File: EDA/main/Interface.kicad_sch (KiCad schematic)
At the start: 16 parts, among them J1 12402012E212A, U1 TF03-TD9P

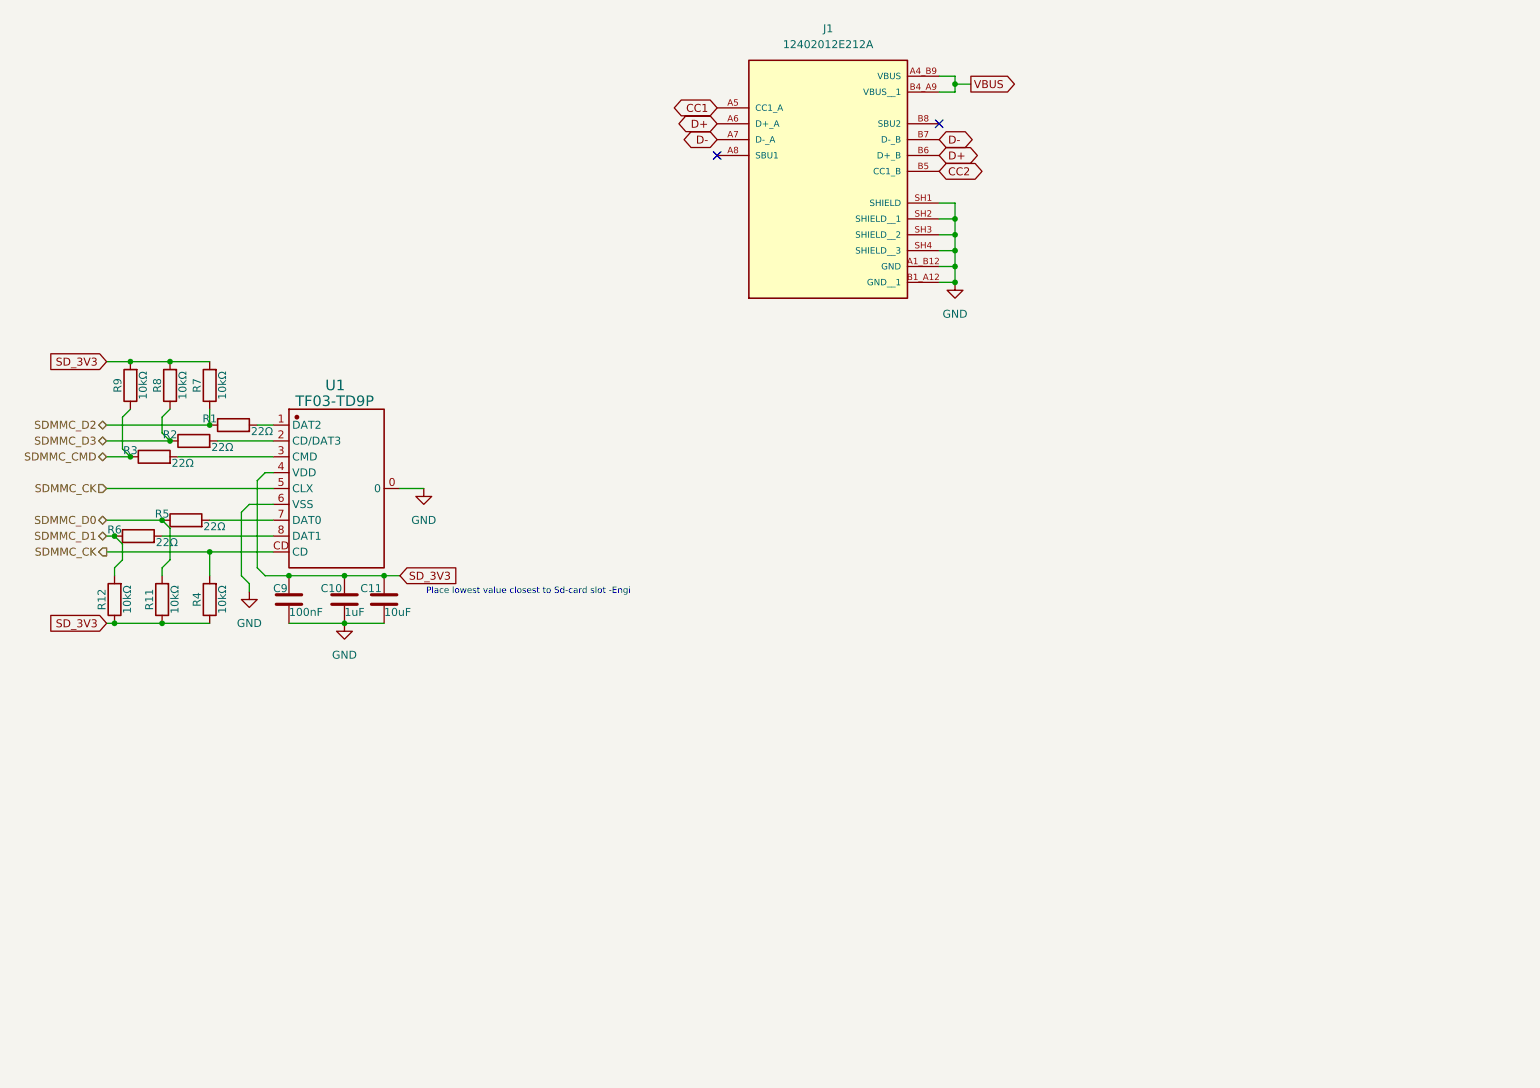
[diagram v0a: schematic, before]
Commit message: Project restructure, and added a bottom assembly PCB.
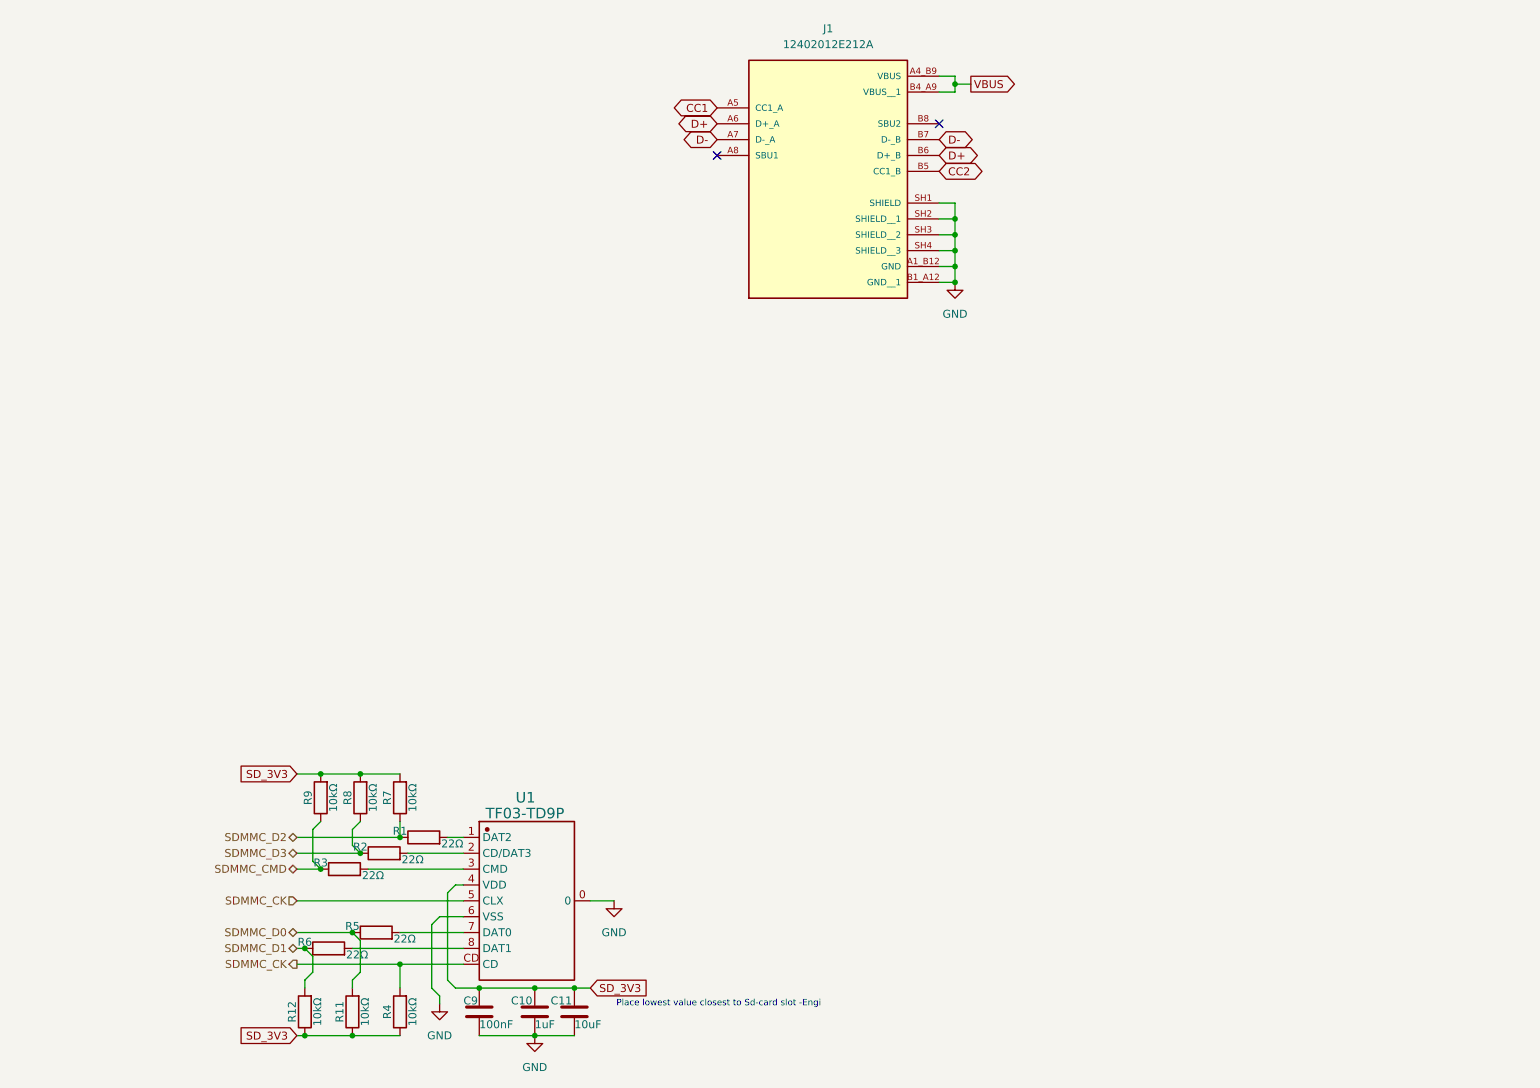
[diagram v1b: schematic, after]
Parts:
- C10, C11: footprint (none) -> Capacitor_SMD:C_0603_1608Metric
- C9: footprint (none) -> Capacitor_SMD:C_0402_1005Metric
- R1, R11, R12, R2, R3, R4, R5, R6, R7, R8, R9: footprint (none) -> Resistor_SMD:R_0402_1005Metric
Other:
- moved on the sheet: C10, C11, C9, R1, R11, R12, R2, R3, R4, R5, R6, R7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

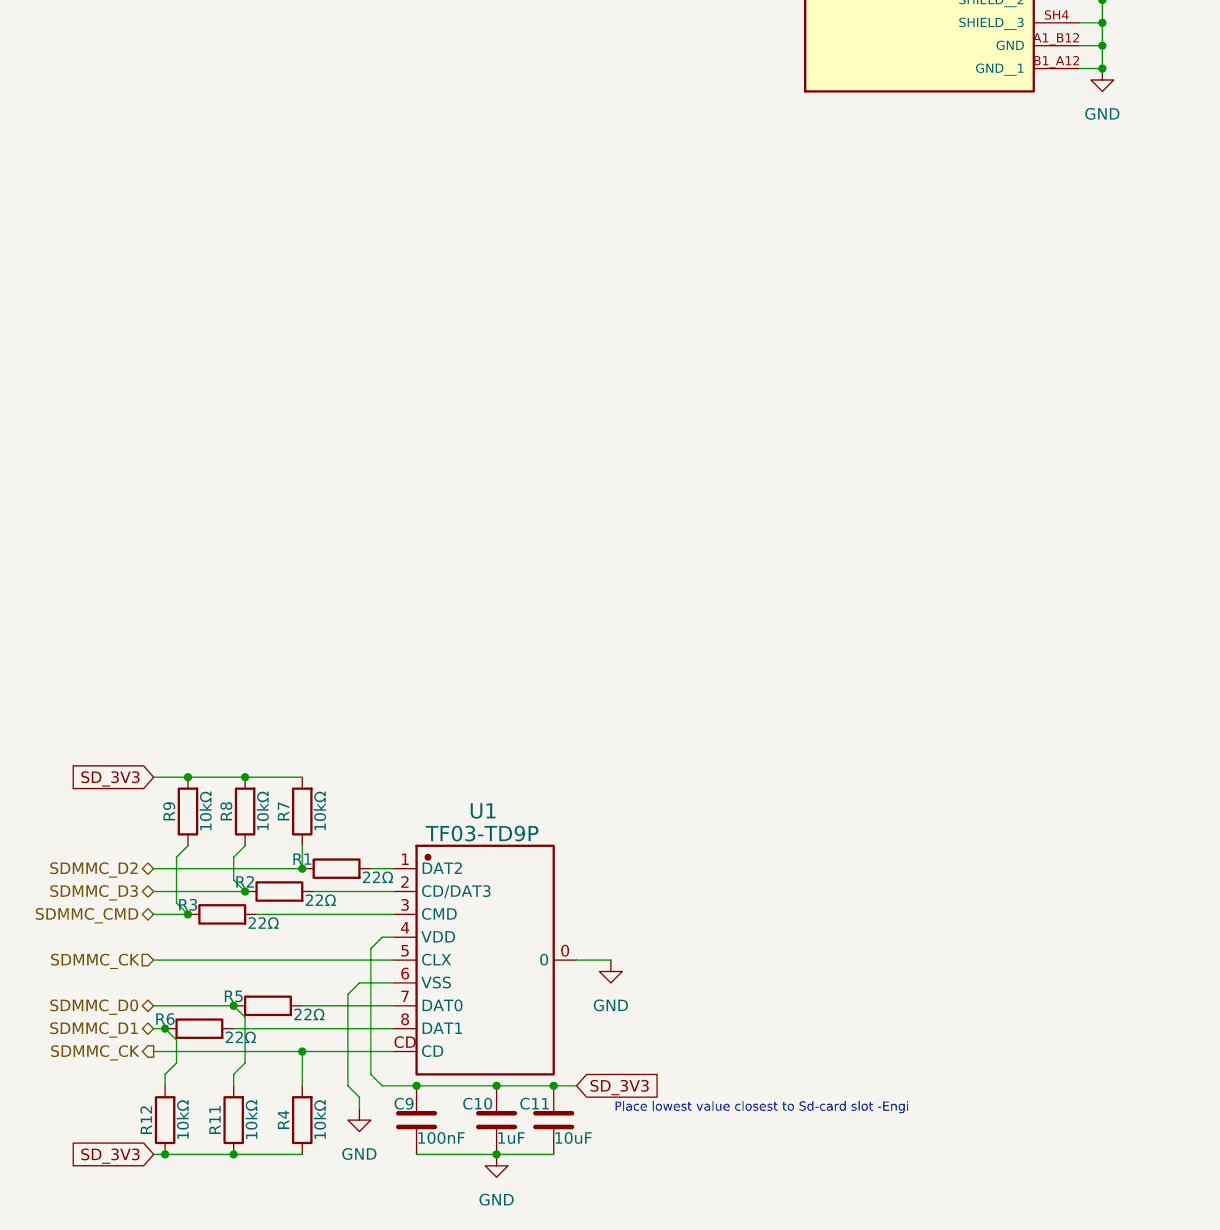
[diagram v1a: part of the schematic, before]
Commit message: Assigned CS and INT from sensors, and added SWD to PWR-MCU and CORE-MCU
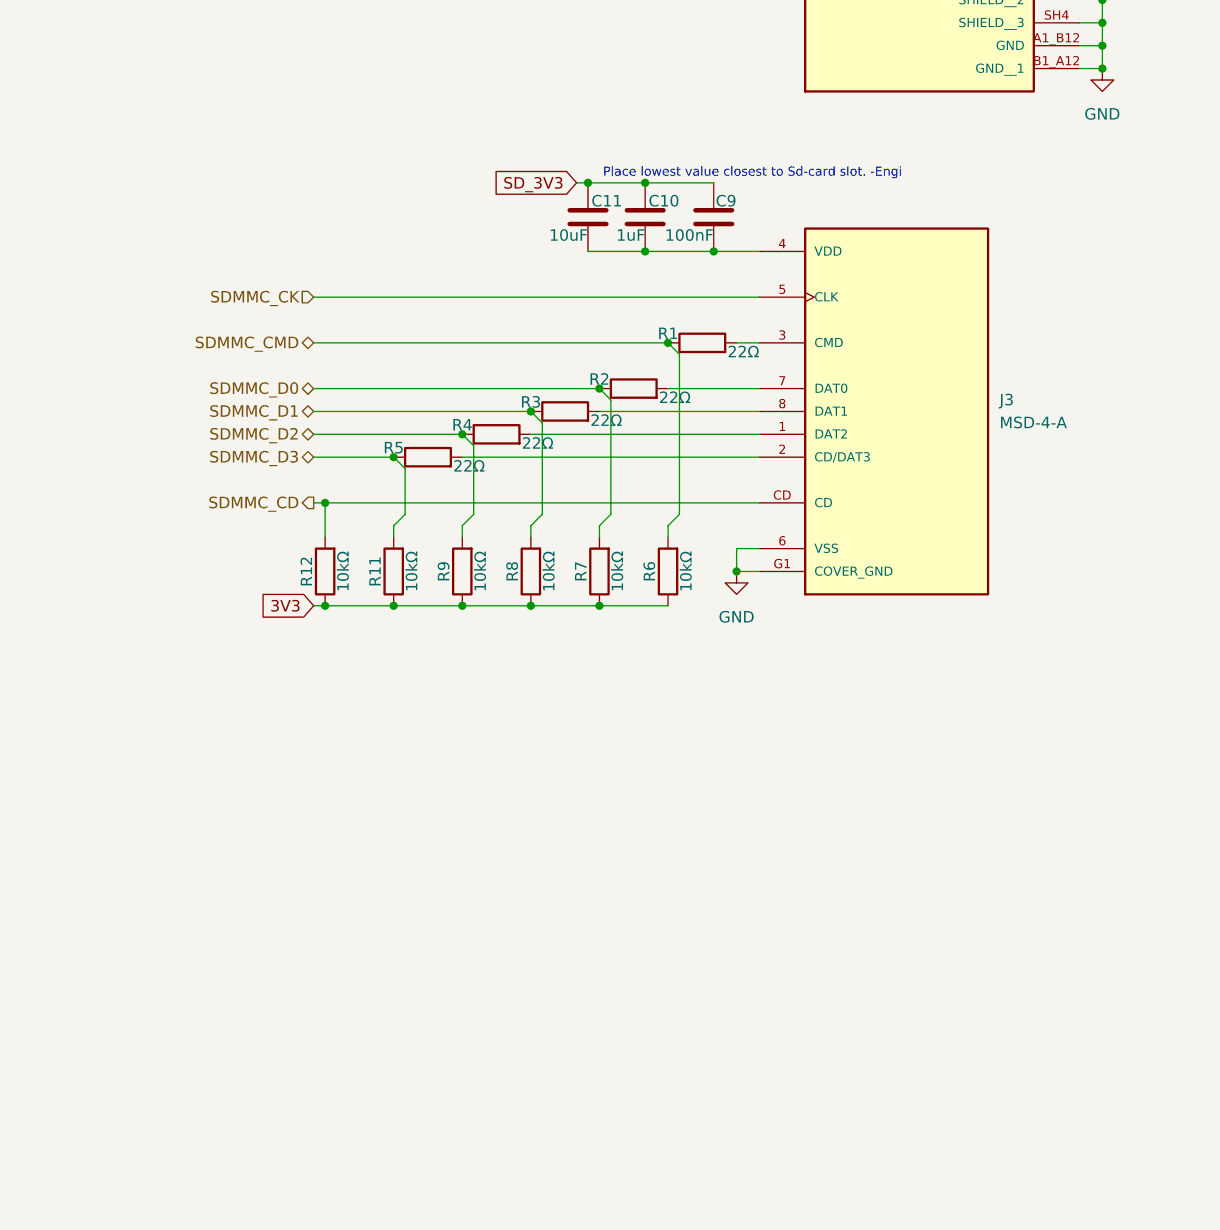
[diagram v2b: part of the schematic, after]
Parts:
- removed U1: TF03-TD9P, symbol TF03-TD9P
- added J3: MSD-4-A, CANSAT-lib:CUI_MSD-4-A, symbol CANSAT-lib:MSD-4-A
- renumbered R5 to R4, R6 to R5, R4 to R6
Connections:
- net SDMMC_CK: now also J3.5 (CLK); no longer R6.2
- net SDMMC_CMD: now also R1.1, R6.2; no longer R3.1, R9.1
- net SDMMC_D0: now also R2.1, R7.2; no longer R11.2, R4.1
- net SDMMC_D1: now also R3.1, R8.2; no longer R12.2, R5.1
- net SDMMC_D2: now also R4.1, R9.2; no longer R1.1, R7.1
- net SDMMC_D3: now also R11.2, R5.1; no longer R2.1, R8.1
- net SD_3V3: no longer R11.1, R12.1, R6.1, R7.2, R8.2, R9.2
- net at R5.2: now also J3.2 (CD/DAT3)
- net at R3.2: now also J3.8 (DAT1)
- net at R1.2: now also J3.3 (CMD)
- net at R2.2: now also J3.7 (DAT0)
- net at R4.2: now also J3.1 (DAT2)
- net GND renamed COVER_GND
- net COVER_GND: now also J3.6 (VSS), J3.G1 (COVER_GND), J3.G2 (COVER_GND), J3.G3 (COVER_GND), J3.G4 (COVER_GND); no longer C10.2, C11.2, C9.2
- new net: C10.2, C11.2, C9.2, J3.4 (VDD)
- new net 3V3: R11.1, R12.1, R6.1, R7.1, R8.1, R9.1
- new net SDMMC_CD: J3.CD, R12.2
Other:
- note added: "Place lowest value closest to Sd-card slot. -Engi"
- note removed: "Place lowest value closest to Sd-card slot -Engi"
- moved on the sheet: C10, C11, C9, R1, R11, R12, R2, R3, R4, R5, R6, R7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

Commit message: Uploaded work
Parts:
- added RF1: ~, CANSAT-lib:SI4463-MODULE, symbol CANSAT-lib:SI4463-Module
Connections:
- net SD_3V3 is gone; now on net 3V3: C10.1, C11.1, C9.1

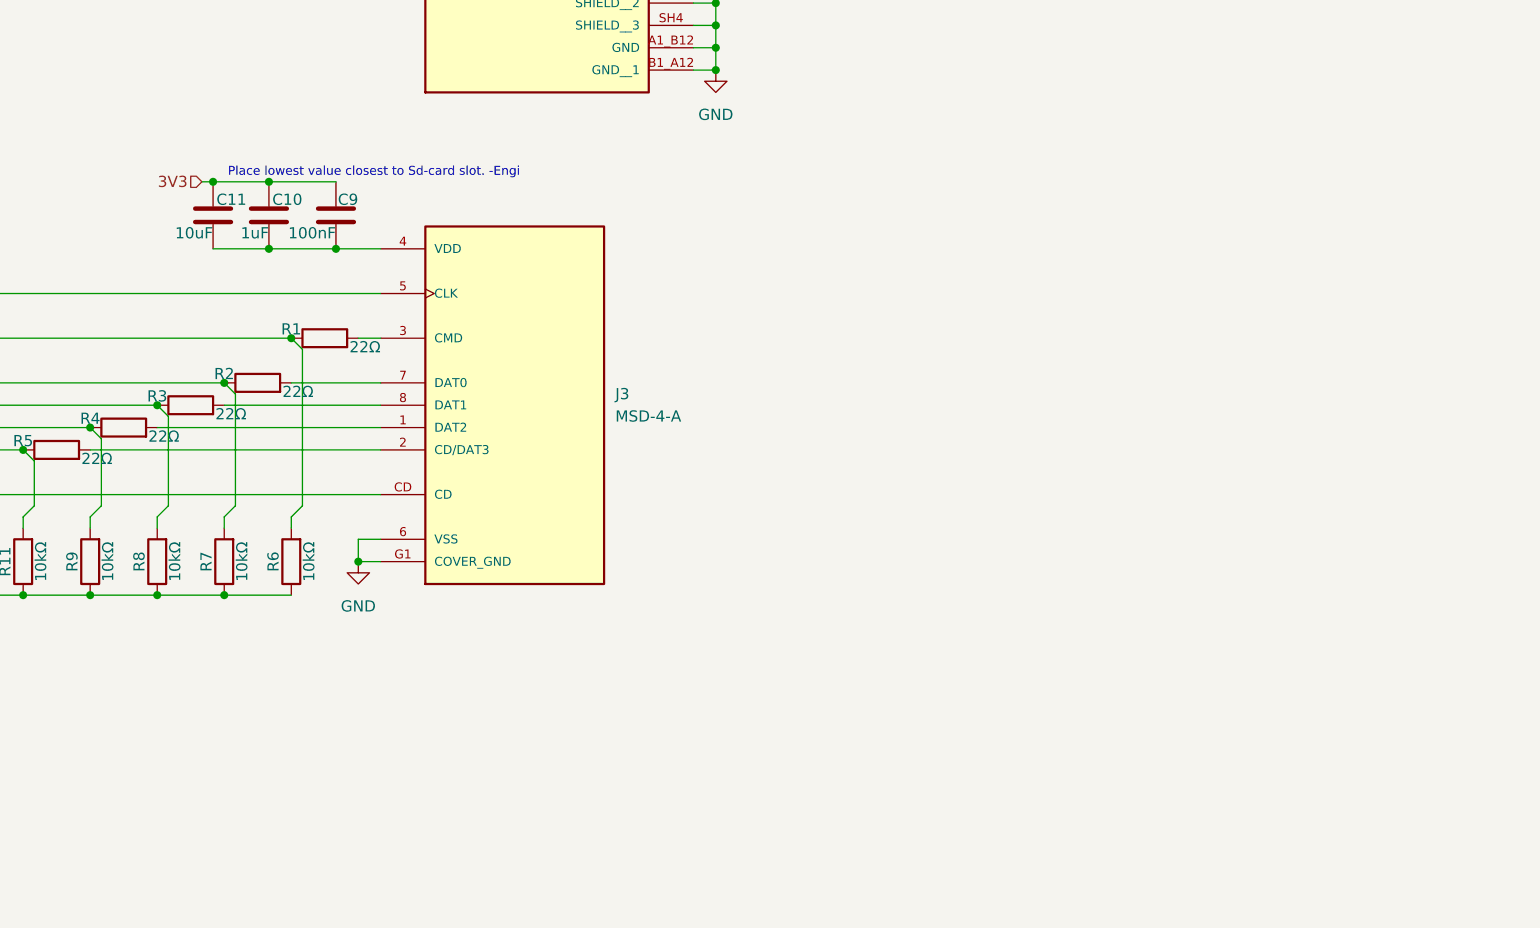
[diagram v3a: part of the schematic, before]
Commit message: Added GNSS and SIM800L
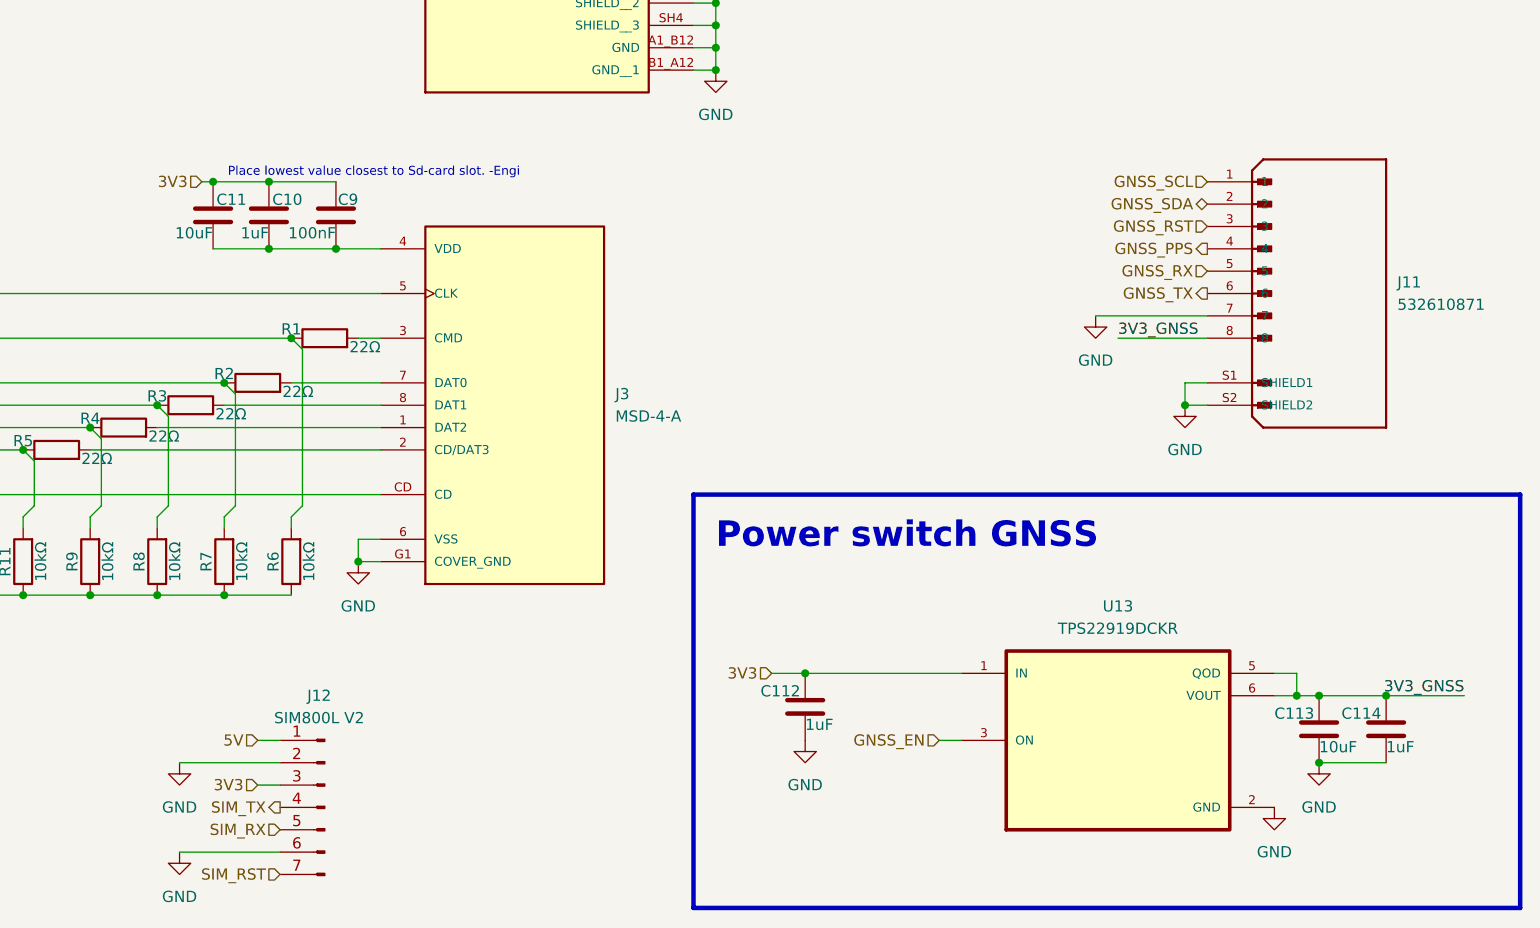
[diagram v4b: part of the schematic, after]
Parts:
- added C112, C114: 1uF, Capacitor_SMD:C_0603_1608Metric, symbol Device:C
- added C113: 10uF, Capacitor_SMD:C_0603_1608Metric, symbol Device:C
- added J11: 532610871, CANSAT-lib:MOLEX_532610871, symbol CANSAT-lib:532610871
- added J12: SIM800L V2, CANSAT-lib:PinHeader_1x07_P2.54mm_Vertical, symbol CANSAT-lib:Conn_01x07_Pin
- added U13: TPS22919DCKR, CANSAT-lib:SOT65P210X110-6N, symbol CANSAT-lib:TPS22919DCKR
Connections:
- net 3V3: now also C112.1, J12.3 (Pin_3), U13.1 (IN)
- net COVER_GND: now also C112.2, C113.2, C114.2, J11.7, J11.S1 (SHIELD1), J11.S2 (SHIELD2), J12.2 (Pin_2), J12.6 (Pin_6), U13.2 (GND)
- new net 3V3_GNSS: C113.1, C114.1, J11.8, U13.5 (QOD), U13.6 (VOUT)
- new net 5V: J12.1 (Pin_1)
- new net GNSS_EN: U13.3 (ON)
- new net GNSS_PPS: J11.4
- new net GNSS_RST: J11.3
- new net GNSS_RX: J11.5
- new net GNSS_SCL: J11.1
- new net GNSS_SDA: J11.2
- new net GNSS_TX: J11.6
- new net SIM_RST: J12.7 (Pin_7)
- new net SIM_RX: J12.5 (Pin_5)
- new net SIM_TX: J12.4 (Pin_4)
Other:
- note added: "Power switch GNSS"
